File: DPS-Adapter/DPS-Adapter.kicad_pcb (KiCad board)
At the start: 2 copper layers, 4 parts, among them J1 Conn_01x04, J2 Conn_01x04, J3 Conn_01x04, J4 Conn_01x04

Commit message: adapter finally routed
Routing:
- net /a4: track 0.00 -> 7.62 mm
- net /a3: track 0.00 -> 7.62 mm
- net /a2: track 0.00 -> 7.62 mm
- net /a1: track 0.00 -> 7.62 mm
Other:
- board outline added: 11.4 x 11.4 mm
- net class Power added: clearance 0.2, trace_width 0.5, via_dia 0.6, via_drill 0.4
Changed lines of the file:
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@@
     (links 12)
     (no_connects 0)
-    (area 0 0 0 0)
+    (area 150.419999 99.619999 162.000001 111.200001)
     (thickness 1.6)
-    (drawings 0)
-    (tracks 0)
+    (drawings 4)
+    (tracks 12)
     (zones 0)
     (modules 4)
@@
     (pad_to_mask_clearance 0.2)
     (aux_axis_origin 0 0)
-    (visible_elements FFFFFF7F)
+    (visible_elements 7FFFFFFF)
     (pcbplotparams
       (layerselection 0x00030_80000001)
@@
     (uvia_dia 0.3)
     (uvia_drill 0.1)
+  )
+  (net_class Power ""
+    (clearance 0.2)
+    (trace_width 0.5)
+    (via_dia 0.6)
+    (via_drill 0.4)
+    (uvia_dia 0.3)
+    (uvia_drill 0.1)
     (add_net /a1)
     (add_net /a2)
@@
     )
   )
+  (gr_line (start 150.495 111.125) (end 150.495 99.695) (layer Edge.Cuts) (width 0.15))
+  (gr_line (start 161.925 111.125) (end 150.495 111.125) (layer Edge.Cuts) (width 0.15))
+  (gr_line (start 161.925 99.695) (end 161.925 111.125) (layer Edge.Cuts) (width 0.15))
+  (gr_line (start 150.495 99.695) (end 161.925 99.695) (layer Edge.Cuts) (width 0.15))
+  (segment (start 157.48 101.6) (end 160.02 101.6) (width 0.5) (layer B.Cu) (net 1))
+  (segment (start 154.94 101.6) (end 157.48 101.6) (width 0.5) (layer B.Cu) (net 1))
+  (segment (start 152.4 101.6) (end 154.94 101.6) (width 0.5) (layer B.Cu) (net 1))
+  (segment (start 154.94 104.14) (end 152.4 104.14) (width 0.5) (layer B.Cu) (net 2))
+  (segment (start 157.48 104.14) (end 154.94 104.14) (width 0.5) (layer B.Cu) (net 2))
+  (segment (start 160.02 104.14) (end 157.48 104.14) (width 0.5) (layer B.Cu) (net 2))
+  (segment (start 157.48 106.68) (end 160.02 106.68) (width 0.5) (layer B.Cu) (net 3))
+  (segment (start 154.94 106.68) (end 157.48 106.68) (width 0.5) (layer B.Cu) (net 3))
+  (segment (start 152.4 106.68) (end 154.94 106.68) (width 0.5) (layer B.Cu) (net 3))
+  (segment (start 154.94 109.22) (end 152.4 109.22) (width 0.5) (layer B.Cu) (net 4))
+  (segment (start 157.48 109.22) (end 154.94 109.22) (width 0.5) (layer B.Cu) (net 4))
+  (segment (start 160.02 109.22) (end 157.48 109.22) (width 0.5) (layer B.Cu) (net 4))
 )

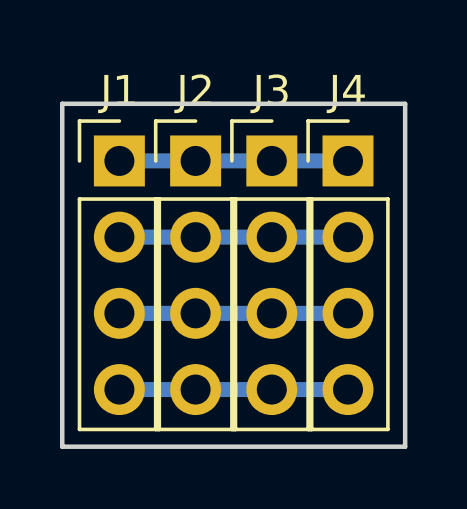
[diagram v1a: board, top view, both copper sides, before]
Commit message: populate changes to archive correct version
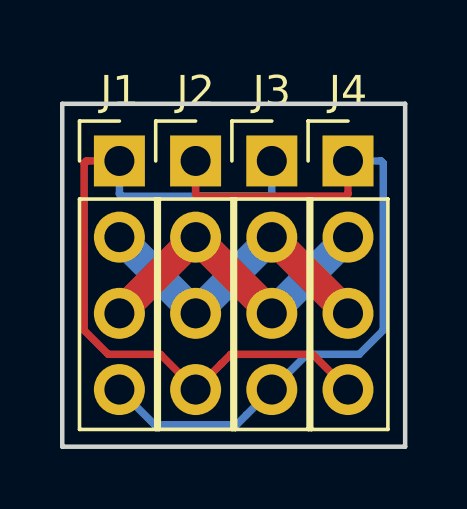
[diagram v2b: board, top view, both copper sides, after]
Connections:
- J1 pad 1: /a1 -> /FS
- J1 pad 2: /a2 -> /GND
- J1 pad 3: /a3 -> /F
- J1 pad 4: /a4 -> /GS
- J2 pad 1: /a1 -> /GS
- J2 pad 2: /a2 -> /F
- J2 pad 3: /a3 -> /GND
- J2 pad 4: /a4 -> /FS
- J3 pad 1: /a1 -> /FS
- J3 pad 2: /a2 -> /GND
- J3 pad 3: /a3 -> /F
- J3 pad 4: /a4 -> /GS
- J4 pad 1: /a1 -> /GS
- J4 pad 2: /a2 -> /F
- J4 pad 3: /a3 -> /GND
- J4 pad 4: /a4 -> /FS
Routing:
- net /FS: track 0.00 -> 24.7 mm
- net /GS: track 0.00 -> 24.7 mm
- net /GND: track 0.00 -> 10.8 mm
- net /F: track 0.00 -> 10.8 mm
- net /a4: track 7.62 -> 0.00 mm
- net /a3: track 7.62 -> 0.00 mm
- net /a2: track 7.62 -> 0.00 mm
- net /a1: track 7.62 -> 0.00 mm
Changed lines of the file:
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@@
     (links 12)
     (no_connects 0)
-    (area 150.419999 99.619999 162.000001 111.200001)
+    (area 147.652381 98.295 164.76762 112.625)
     (thickness 1.6)
     (drawings 4)
-    (tracks 12)
+    (tracks 36)
     (zones 0)
     (modules 4)
@@
       (outputformat 1)
       (mirror false)
-      (drillshape 1)
+      (drillshape 0)
       (scaleselection 1)
       (outputdirectory ""))
   )
   (net 0 "")
-  (net 1 /a1)
-  (net 2 /a2)
-  (net 3 /a3)
-  (net 4 /a4)
+  (net 1 /FS)
+  (net 2 /GND)
+  (net 3 /F)
+  (net 4 /GS)
   (net_class Default "Dies ist die voreingestellte Netzklasse."
     (clearance 0.2)
@@
     (uvia_dia 0.3)
     (uvia_drill 0.1)
+    (add_net /FS)
+    (add_net /GS)
   )
   (net_class Power ""
@@
     (uvia_dia 0.3)
     (uvia_drill 0.1)
-    (add_net /a1)
-    (add_net /a2)
-    (add_net /a3)
-    (add_net /a4)
+    (add_net /F)
+    (add_net /GND)
   )
   (module Socket_Strips:Socket_Strip_Straight_1x04_Pitch2.54mm (layer F.Cu)
@@
     )
     (pad 1 thru_hole rect (at 0 0) (size 1.7 1.7) (drill 1) (layers *.Cu *.Mask)
-      (net 1 /a1))
+      (net 1 /FS))
     (pad 2 thru_hole oval (at 0 2.54) (size 1.7 1.7) (drill 1) (layers *.Cu *.Mask)
-      (net 2 /a2))
+      (net 2 /GND))
     (pad 3 thru_hole oval (at 0 5.08) (size 1.7 1.7) (drill 1) (layers *.Cu *.Mask)
-      (net 3 /a3))
+      (net 3 /F))
     (pad 4 thru_hole oval (at 0 7.62) (size 1.7 1.7) (drill 1) (layers *.Cu *.Mask)
-      (net 4 /a4))
+      (net 4 /GS))
     (model ${KISYS3DMOD}/Socket_Strips.3dshapes/Socket_Strip_Straight_1x04_Pitch2.54mm.wrl
       (at (xyz 0 -0.15 0))
@@
     )
     (pad 1 thru_hole rect (at 0 0) (size 1.7 1.7) (drill 1) (layers *.Cu *.Mask)
-      (net 1 /a1))
+      (net 4 /GS))
     (pad 2 thru_hole oval (at 0 2.54) (size 1.7 1.7) (drill 1) (layers *.Cu *.Mask)
-      (net 2 /a2))
+      (net 3 /F))
     (pad 3 thru_hole oval (at 0 5.08) (size 1.7 1.7) (drill 1) (layers *.Cu *.Mask)
-      (net 3 /a3))
+      (net 2 /GND))
     (pad 4 thru_hole oval (at 0 7.62) (size 1.7 1.7) (drill 1) (layers *.Cu *.Mask)
-      (net 4 /a4))
+      (net 1 /FS))
     (model ${KISYS3DMOD}/Socket_Strips.3dshapes/Socket_Strip_Straight_1x04_Pitch2.54mm.wrl
       (at (xyz 0 -0.15 0))
@@
     )
     (pad 1 thru_hole rect (at 0 0) (size 1.7 1.7) (drill 1) (layers *.Cu *.Mask)
-      (net 1 /a1))
+      (net 1 /FS))
     (pad 2 thru_hole oval (at 0 2.54) (size 1.7 1.7) (drill 1) (layers *.Cu *.Mask)
-      (net 2 /a2))
+      (net 2 /GND))
     (pad 3 thru_hole oval (at 0 5.08) (size 1.7 1.7) (drill 1) (layers *.Cu *.Mask)
-      (net 3 /a3))
+      (net 3 /F))
     (pad 4 thru_hole oval (at 0 7.62) (size 1.7 1.7) (drill 1) (layers *.Cu *.Mask)
-      (net 4 /a4))
+      (net 4 /GS))
     (model ${KISYS3DMOD}/Socket_Strips.3dshapes/Socket_Strip_Straight_1x04_Pitch2.54mm.wrl
       (at (xyz 0 -0.15 0))
@@
     )
     (pad 1 thru_hole rect (at 0 0) (size 1.7 1.7) (drill 1) (layers *.Cu *.Mask)
-      (net 1 /a1))
+      (net 4 /GS))
     (pad 2 thru_hole oval (at 0 2.54) (size 1.7 1.7) (drill 1) (layers *.Cu *.Mask)
-      (net 2 /a2))
+      (net 3 /F))
     (pad 3 thru_hole oval (at 0 5.08) (size 1.7 1.7) (drill 1) (layers *.Cu *.Mask)
-      (net 3 /a3))
+      (net 2 /GND))
     (pad 4 thru_hole oval (at 0 7.62) (size 1.7 1.7) (drill 1) (layers *.Cu *.Mask)
-      (net 4 /a4))
+      (net 1 /FS))
     (model ${KISYS3DMOD}/Socket_Strips.3dshapes/Socket_Strip_Straight_1x04_Pitch2.54mm.wrl
       (at (xyz 0 -0.15 0))
@@
   (gr_line (start 161.925 99.695) (end 161.925 111.125) (layer Edge.Cuts) (width 0.15))
   (gr_line (start 150.495 99.695) (end 161.925 99.695) (layer Edge.Cuts) (width 0.15))
-  (segment (start 157.48 101.6) (end 160.02 101.6) (width 0.5) (layer B.Cu) (net 1))
-  (segment (start 154.94 101.6) (end 157.48 101.6) (width 0.5) (layer B.Cu) (net 1))
-  (segment (start 152.4 101.6) (end 154.94 101.6) (width 0.5) (layer B.Cu) (net 1))
-  (segment (start 154.94 104.14) (end 152.4 104.14) (width 0.5) (layer B.Cu) (net 2))
-  (segment (start 157.48 104.14) (end 154.94 104.14) (width 0.5) (layer B.Cu) (net 2))
-  (segment (start 160.02 104.14) (end 157.48 104.14) (width 0.5) (layer B.Cu) (net 2))
-  (segment (start 157.48 106.68) (end 160.02 106.68) (width 0.5) (layer B.Cu) (net 3))
-  (segment (start 154.94 106.68) (end 157.48 106.68) (width 0.5) (layer B.Cu) (net 3))
-  (segment (start 152.4 106.68) (end 154.94 106.68) (width 0.5) (layer B.Cu) (net 3))
-  (segment (start 154.94 109.22) (end 152.4 109.22) (width 0.5) (layer B.Cu) (net 4))
-  (segment (start 157.48 109.22) (end 154.94 109.22) (width 0.5) (layer B.Cu) (net 4))
-  (segment (start 160.02 109.22) (end 157.48 109.22) (width 0.5) (layer B.Cu) (net 4))
+  (segment (start 152.4 101.6) (end 152.4 102.7) (width 0.25) (layer B.Cu) (net 1))
+  (segment (start 152.4 102.7) (end 152.475001 102.775001) (width 0.25) (layer B.Cu) (net 1))
+  (segment (start 152.475001 102.775001) (end 157.404999 102.775001) (width 0.25) (layer B.Cu) (net 1))
+  (segment (start 157.404999 102.775001) (end 157.48 102.7) (width 0.25) (layer B.Cu) (net 1))
+  (segment (start 157.48 102.7) (end 157.48 101.6) (width 0.25) (layer B.Cu) (net 1))
+  (segment (start 154.94 109.22) (end 153.764999 108.044999) (width 0.25) (layer F.Cu) (net 1))
+  (segment (start 153.764999 108.044999) (end 152.025997 108.044999) (width 0.25) (layer F.Cu) (net 1))
+  (segment (start 152.025997 108.044999) (end 151.224999 107.244001) (width 0.25) (layer F.Cu) (net 1))
+  (segment (start 151.224999 107.244001) (end 151.224999 101.675001) (width 0.25) (layer F.Cu) (net 1))
+  (segment (start 151.224999 101.675001) (end 151.3 101.6) (width 0.25) (layer F.Cu) (net 1))
+  (segment (start 151.3 101.6) (end 152.4 101.6) (width 0.25) (layer F.Cu) (net 1))
+  (segment (start 160.02 109.22) (end 158.844999 108.044999) (width 0.25) (layer F.Cu) (net 1))
+  (segment (start 155.789999 108.370001) (end 154.94 109.22) (width 0.25) (layer F.Cu) (net 1))
+  (segment (start 158.844999 108.044999) (end 156.115001 108.044999) (width 0.25) (layer F.Cu) (net 1))
+  (segment (start 156.115001 108.044999) (end 155.789999 108.370001) (width 0.25) (layer F.Cu) (net 1))
+  (segment (start 157.48 104.14) (end 160.02 106.68) (width 1) (layer F.Cu) (net 2))
+  (segment (start 154.94 106.68) (end 157.48 104.14) (width 1) (layer B.Cu) (net 2))
+  (segment (start 152.4 104.14) (end 154.94 106.68) (width 1) (layer B.Cu) (net 2))
+  (segment (start 157.48 106.68) (end 160.02 104.14) (width 1) (layer B.Cu) (net 3))
+  (segment (start 154.94 104.14) (end 157.48 106.68) (width 1) (layer F.Cu) (net 3))
+  (segment (start 152.4 106.68) (end 154.94 104.14) (width 1) (layer F.Cu) (net 3))
+  (segment (start 160.02 101.6) (end 160.02 102.7) (width 0.25) (layer F.Cu) (net 4))
+  (segment (start 160.02 102.7) (end 159.944999 102.775001) (width 0.25) (layer F.Cu) (net 4))
+  (segment (start 159.944999 102.775001) (end 155.015001 102.775001) (width 0.25) (layer F.Cu) (net 4))
+  (segment (start 155.015001 102.775001) (end 154.94 102.7) (width 0.25) (layer F.Cu) (net 4))
+  (segment (start 154.94 102.7) (end 154.94 101.6) (width 0.25) (layer F.Cu) (net 4))
+  (segment (start 157.48 109.22) (end 158.655001 108.044999) (width 0.25) (layer B.Cu) (net 4))
+  (segment (start 158.655001 108.044999) (end 160.394003 108.044999) (width 0.25) (layer B.Cu) (net 4))
+  (segment (start 160.394003 108.044999) (end 161.195001 107.244001) (width 0.25) (layer B.Cu) (net 4))
+  (segment (start 161.195001 107.244001) (end 161.195001 101.675001) (width 0.25) (layer B.Cu) (net 4))
+  (segment (start 161.195001 101.675001) (end 161.12 101.6) (width 0.25) (layer B.Cu) (net 4))
+  (segment (start 161.12 101.6) (end 160.02 101.6) (width 0.25) (layer B.Cu) (net 4))
+  (segment (start 152.4 109.22) (end 153.575001 110.395001) (width 0.25) (layer B.Cu) (net 4))
+  (segment (start 153.575001 110.395001) (end 156.304999 110.395001) (width 0.25) (layer B.Cu) (net 4))
+  (segment (start 156.304999 110.395001) (end 156.630001 110.069999) (width 0.25) (layer B.Cu) (net 4))
+  (segment (start 156.630001 110.069999) (end 157.48 109.22) (width 0.25) (layer B.Cu) (net 4))
 )
